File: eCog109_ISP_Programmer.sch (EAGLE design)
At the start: 1 part

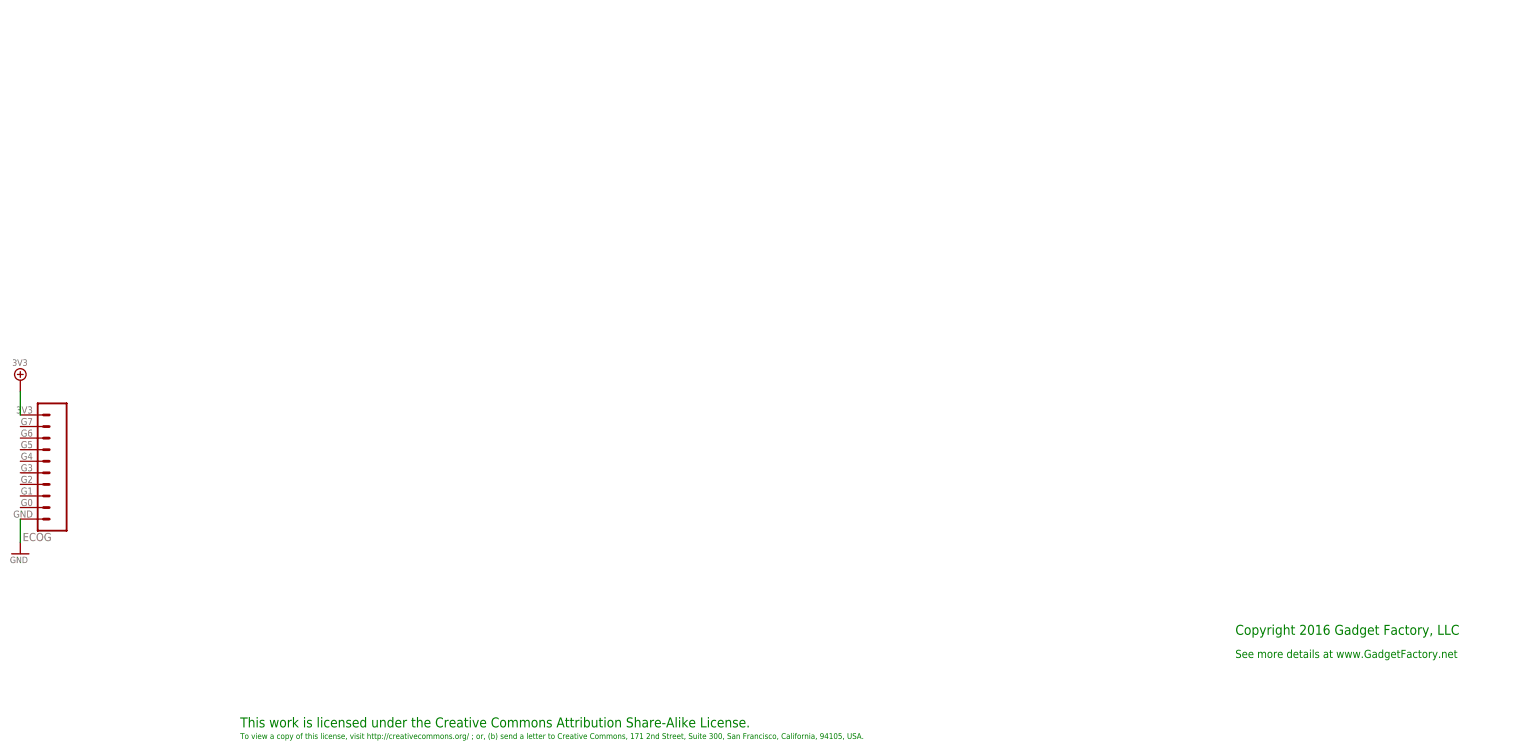
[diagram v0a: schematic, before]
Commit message: Added new eCogs
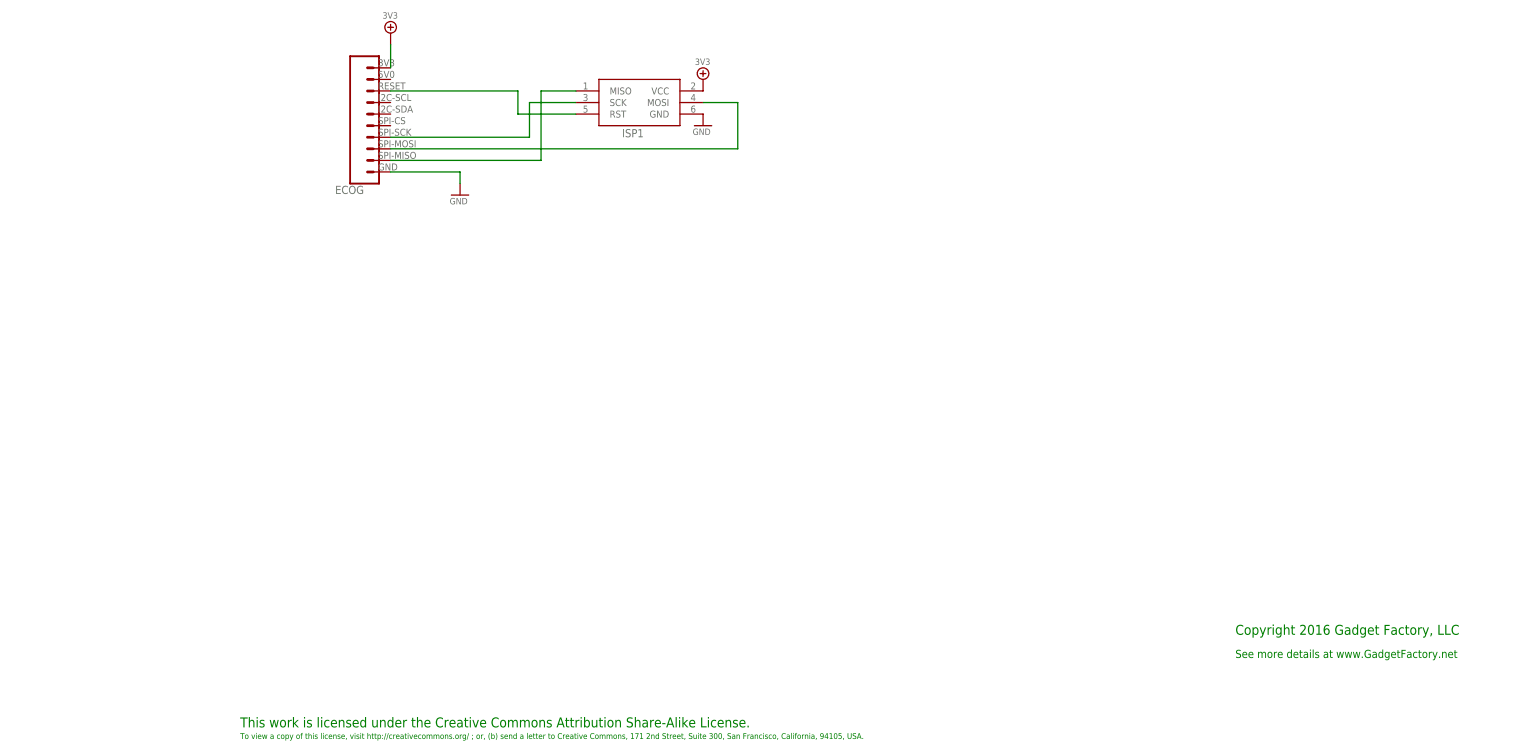
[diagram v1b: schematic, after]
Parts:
- added ISP1: AVRISP-6, adafruit:AVRISP-6
- ECOG: value ECOG_GENERAL_ROWECOG_GENERAL_SMD -> ECOG_BUSES_ROWECOG_BUSES_SMD; device eCogs:ECOG_GENERAL_ROWECOG_GENERAL_SMD -> eCogs:ECOG_BUSES_ROWECOG_BUSES_SMD
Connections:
- new net N$1: ECOG.SPI-MISO@B0, ISP1.MISO
- new net N$2: ECOG.SPI-SCK@B2, ISP1.SCK
- new net N$3: ECOG.RESET@B6, ISP1.RST
- new net N$4: ECOG.SPI-MOSI@B1, ISP1.MOSI
- net 3V3: now also ECOG.3V3@B8, ISP1.VCC; no longer ECOG.3V3
- net GND: now also ECOG.GND@B, ISP1.GND; no longer ECOG.GND
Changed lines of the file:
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@@
 <parts>
 <part name="FRAME1" library="frames" deviceset="A3L-LOC" device=""/>
-<part name="ECOG" library="eCogs" deviceset="ECOG_GENERAL_ROW" device="ECOG_GENERAL_SMD" value="ECOG_GENERAL_ROWECOG_GENERAL_SMD"/>
+<part name="ECOG" library="eCogs" deviceset="ECOG_BUSES_ROW" device="ECOG_BUSES_SMD" value="ECOG_BUSES_ROWECOG_BUSES_SMD"/>
+<part name="GND1" library="eCogs" deviceset="GND" device=""/>
 <part name="3V3_PWR1" library="eCogs" deviceset="3V3" device=""/>
-<part name="GND1" library="eCogs" deviceset="GND" device=""/>
+<part name="ISP1" library="adafruit" deviceset="AVRISP" device="-6"/>
+<part name="GND2" library="eCogs" deviceset="GND" device=""/>
+<part name="3V3_PWR2" library="eCogs" deviceset="3V3" device=""/>
 </parts>
 <sheets>
@@
 <instances>
 <instance part="FRAME1" gate="G$1" x="0" y="0"/>
-<instance part="ECOG" gate="ECOG_GENERAL" x="55.88" y="53.34"/>
-<instance part="3V3_PWR1" gate="A" x="50.8" y="86.36"/>
-<instance part="GND1" gate="A" x="50.8" y="48.26"/>
+<instance part="ECOG" gate="ECOG_BUSES" x="124.46" y="129.54"/>
+<instance part="GND1" gate="A" x="147.32" y="127"/>
+<instance part="3V3_PWR1" gate="A" x="132.08" y="162.56"/>
+<instance part="ISP1" gate="G$1" x="185.42" y="147.32"/>
+<instance part="GND2" gate="A" x="200.66" y="142.24"/>
+<instance part="3V3_PWR2" gate="A" x="200.66" y="152.4"/>
 </instances>
 <busses>
 </busses>
 <nets>
+<net name="GND" class="0">
+<segment>
+<pinref part="ECOG" gate="ECOG_BUSES" pin="GND@B"/>
+<pinref part="GND1" gate="A" pin="GND"/>
+<wire x1="132.08" y1="132.08" x2="147.32" y2="132.08" width="0.2032" layer="91"/>
+<wire x1="147.32" y1="132.08" x2="147.32" y2="129.54" width="0.2032" layer="91"/>
+</segment>
+<segment>
+<pinref part="ISP1" gate="G$1" pin="GND"/>
+<pinref part="GND2" gate="A" pin="GND"/>
+</segment>
+</net>
 <net name="3V3" class="0">
 <segment>
-<pinref part="ECOG" gate="ECOG_GENERAL" pin="3V3"/>
 <pinref part="3V3_PWR1" gate="A" pin="3V3"/>
-<wire x1="50.8" y1="83.82" x2="50.8" y2="78.74" width="0.1524" layer="91"/>
+<pinref part="ECOG" gate="ECOG_BUSES" pin="3V3@B8"/>
+<wire x1="132.08" y1="160.02" x2="132.08" y2="154.94" width="0.2032" layer="91"/>
+</segment>
+<segment>
+<pinref part="ISP1" gate="G$1" pin="VCC"/>
+<pinref part="3V3_PWR2" gate="A" pin="3V3"/>
 </segment>
 </net>
-<net name="GND" class="0">
+<net name="N$1" class="0">
 <segment>
-<pinref part="ECOG" gate="ECOG_GENERAL" pin="GND"/>
-<pinref part="GND1" gate="A" pin="GND"/>
-<wire x1="50.8" y1="55.88" x2="50.8" y2="50.8" width="0.2032" layer="91"/>
+<pinref part="ECOG" gate="ECOG_BUSES" pin="SPI-MISO@B0"/>
+<wire x1="132.08" y1="134.62" x2="165.1" y2="134.62" width="0.2032" layer="91"/>
+<wire x1="165.1" y1="134.62" x2="165.1" y2="149.86" width="0.2032" layer="91"/>
+<pinref part="ISP1" gate="G$1" pin="MISO"/>
+<wire x1="165.1" y1="149.86" x2="172.72" y2="149.86" width="0.2032" layer="91"/>
 </segment>
 </net>
+<net name="N$2" class="0">
+<segment>
+<pinref part="ECOG" gate="ECOG_BUSES" pin="SPI-SCK@B2"/>
+<wire x1="132.08" y1="139.7" x2="162.56" y2="139.7" width="0.2032" layer="91"/>
+<wire x1="162.56" y1="139.7" x2="162.56" y2="147.32" width="0.2032" layer="91"/>
+<pinref part="ISP1" gate="G$1" pin="SCK"/>
+<wire x1="162.56" y1="147.32" x2="172.72" y2="147.32" width="0.2032" layer="91"/>
+</segment>
+</net>
+<net name="N$3" class="0">
+<segment>
+<pinref part="ECOG" gate="ECOG_BUSES" pin="RESET@B6"/>
+<wire x1="132.08" y1="149.86" x2="160.02" y2="149.86" width="0.2032" layer="91"/>
+<wire x1="160.02" y1="149.86" x2="160.02" y2="144.78" width="0.2032" layer="91"/>
+<pinref part="ISP1" gate="G$1" pin="RST"/>
+<wire x1="160.02" y1="144.78" x2="172.72" y2="144.78" width="0.2032" layer="91"/>
+</segment>
+</net>
+<net name="N$4" class="0">
+<segment>
+<pinref part="ECOG" gate="ECOG_BUSES" pin="SPI-MOSI@B1"/>
+<wire x1="132.08" y1="137.16" x2="208.28" y2="137.16" width="0.2032" layer="91"/>
+<wire x1="208.28" y1="137.16" x2="208.28" y2="147.32" width="0.2032" layer="91"/>
+<pinref part="ISP1" gate="G$1" pin="MOSI"/>
+<wire x1="208.28" y1="147.32" x2="200.66" y2="147.32" width="0.2032" layer="91"/>
+</segment>
+</net>
